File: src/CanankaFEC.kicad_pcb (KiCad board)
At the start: 2 copper layers, 24 x 27.9 mm, 26 parts, among them J1 B3B-XH-A, P1 105444-0001, U1 FT232RL, U2 PIC18F25K80

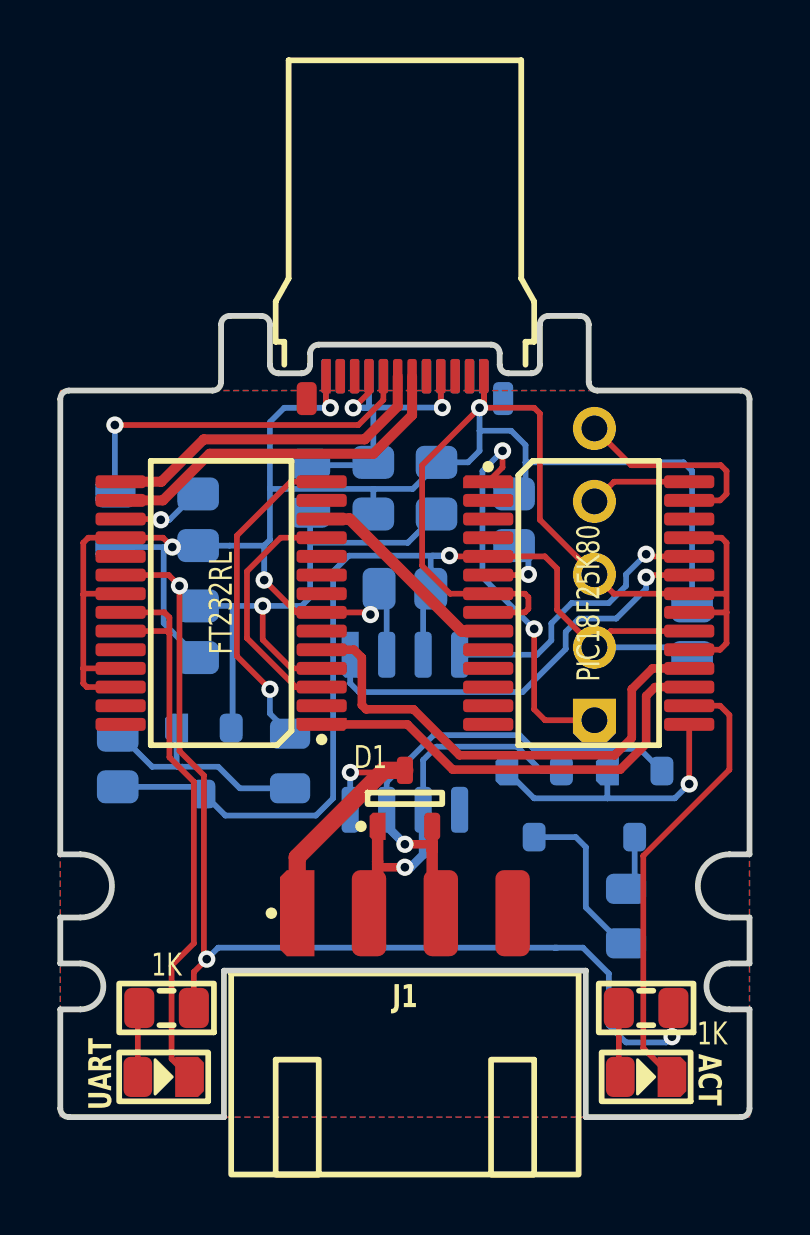
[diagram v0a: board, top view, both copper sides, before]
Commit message: Moved LEDs to bottom side
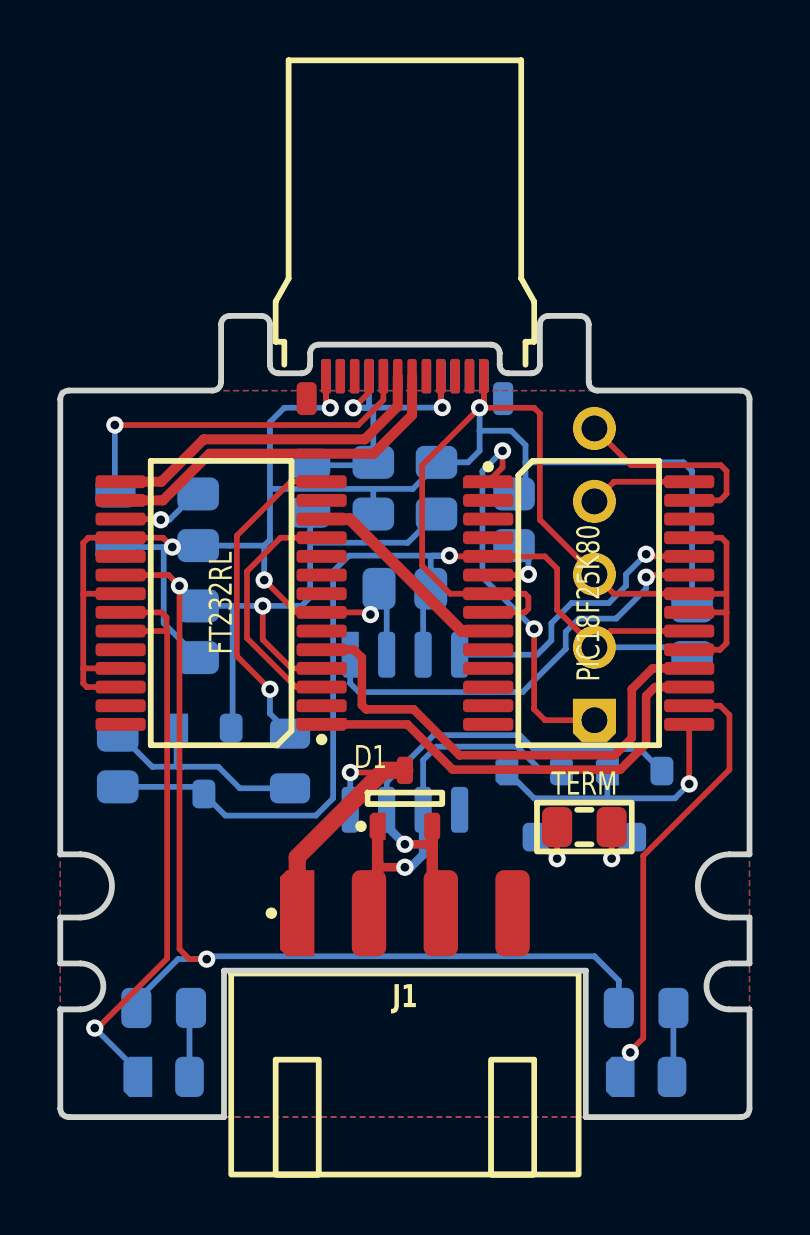
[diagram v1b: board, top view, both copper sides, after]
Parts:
- DS1, DS2, R2, R3: moved to B.Cu
- R1: value 120 -> TERM; moved to F.Cu
- moved R1 3.42 mm to (38.2, 37.8), turned to 0 degrees
- moved R2 0.10 mm to (23.6, 44.1), turned to 0 degrees
- turned DS1 to 0 degrees
- turned DS2 to 0 degrees
- turned R3 to 0 degrees
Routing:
- net CAN_L_TERM: track 5.96 -> 2.71 mm, vias 0 -> 1
- net 5V: track 58.1 -> 55.3 mm, vias 4 -> 3
- net GND: track 111.9 -> 109.8 mm
- net 5V_SW: track 38.9 -> 37.6 mm
- net CANH: track 17.4 -> 16.3 mm
- net LED_ACTIVITY: track 15.8 -> 15.2 mm, vias 0 -> 1
- net LED_UART: track 20.4 -> 20.8 mm, vias 0 -> 1
- net CAN_H_TERM: track 1.92 -> 2.21 mm, vias 0 -> 1

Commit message: Added PWREN pullup and moved LED 5V to switched
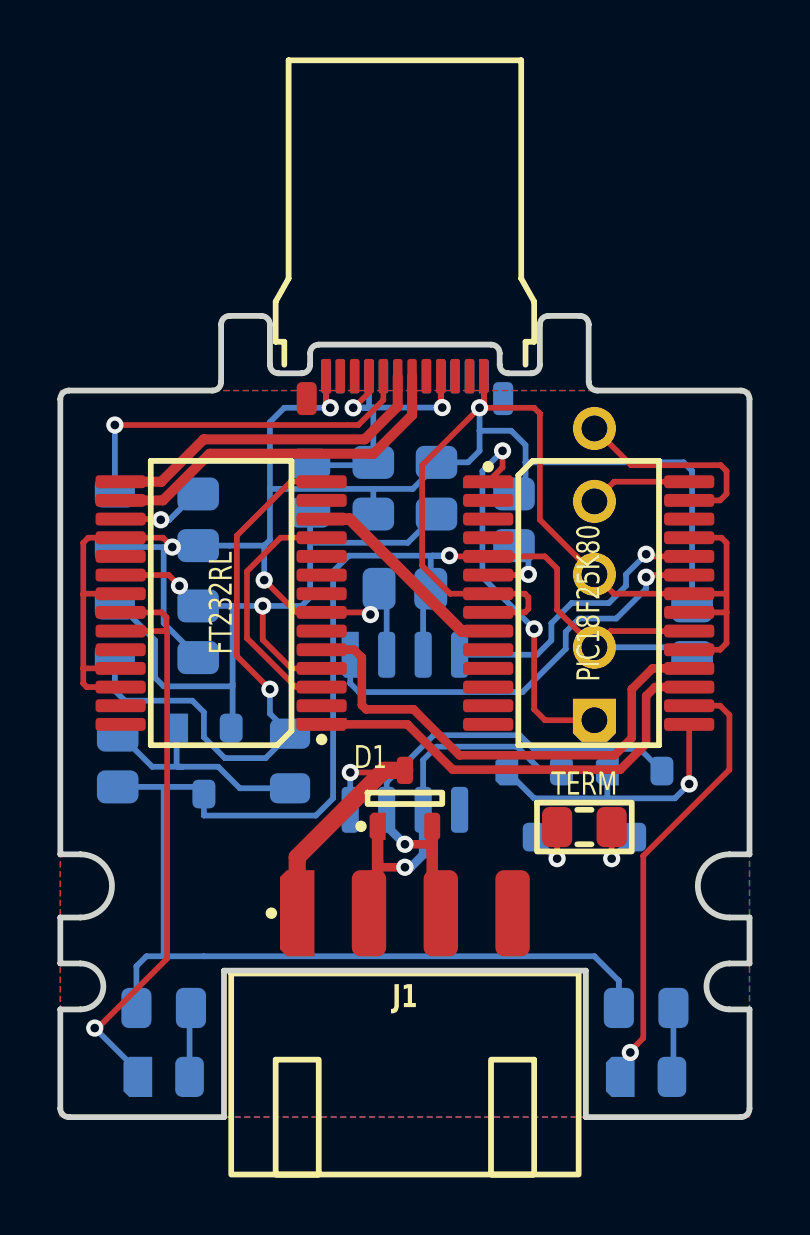
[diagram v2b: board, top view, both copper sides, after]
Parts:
- added R5: 10K, Medo64:R (0805), B.Cu at (21.9, 31.0)
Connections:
- R2 pad 1: 5V -> 5V_SW
- R3 pad 1: 5V -> 5V_SW
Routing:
- net 5V: track 55.3 -> 28.7 mm, vias 3 -> 2
- net 5V_SW: track 37.6 -> 63.4 mm
- net PWREN#: track 11.4 -> 20.4 mm

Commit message: Refactoring copper pour
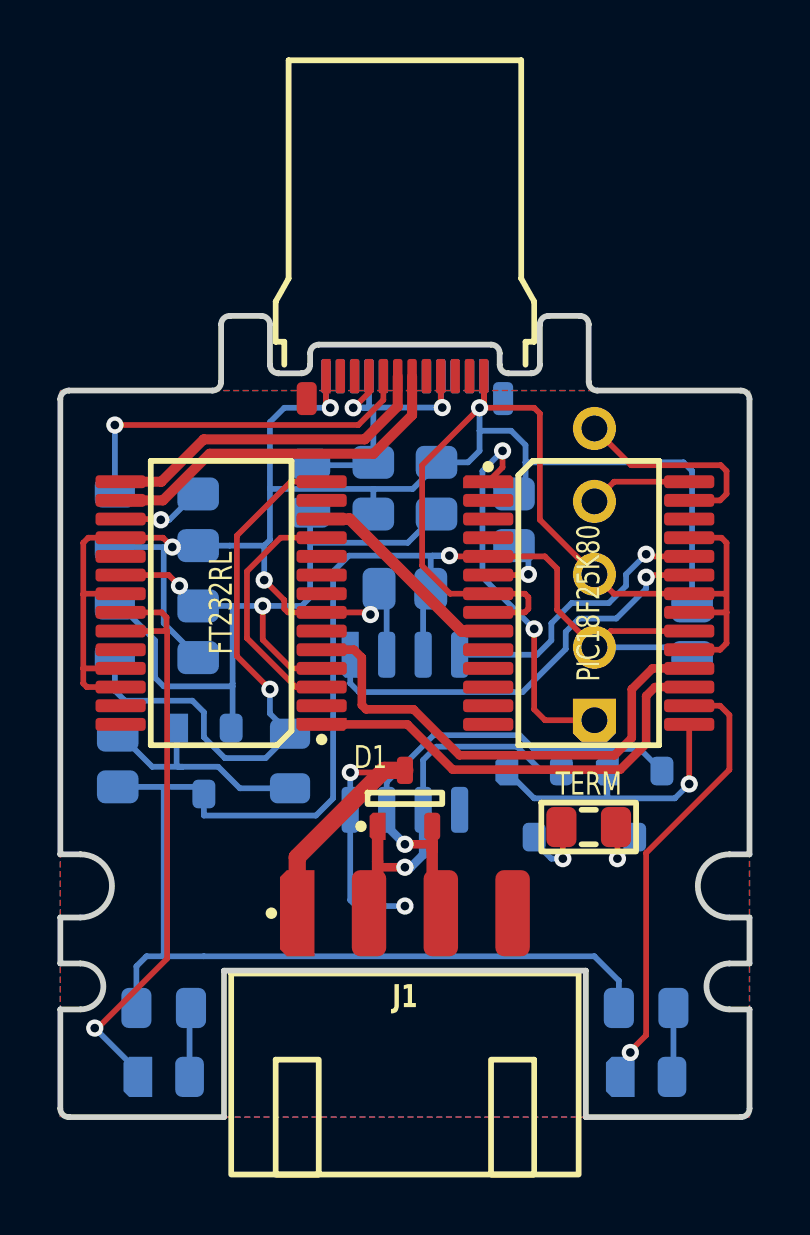
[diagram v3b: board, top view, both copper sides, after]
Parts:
- moved R1 0.15 mm to (38.4, 37.8)
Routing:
- net GND: track 109.8 -> 115.1 mm, vias 6 -> 7
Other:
- rule pad_to_mask_clearance: 0 -> 0.05
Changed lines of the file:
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@@
       (dielectric_constraints no)
     )
-    (pad_to_mask_clearance 0)
+    (pad_to_mask_clearance 0.05)
     (aux_axis_origin 20 20)
     (pcbplotparams
@@
   )
   (footprint "Medo64:R (0805)" (layer "F.Cu")
-    (at 38.25 37.8)
+    (at 38.4 37.8)
     (tags "RESC2013X70N")
     (attr smd)
@@
   (segment (start 36.175 30.325) (end 36.3 30.2) (width 0.2) (layer "F.Cu") (net 7))
   (segment (start 34.9 29.675) (end 33.575 29.675) (width 0.2) (layer "F.Cu") (net 7))
-  (segment (start 29.1 30.325) (end 28.225 30.325) (width 0.2) (layer "F.Cu") (net 7))
   (segment (start 34.75 22.95697) (end 34.75 22.1) (width 0.2) (layer "F.Cu") (net 7))
   (segment (start 22.1 32.275) (end 20.8 32.275) (width 0.2) (layer "F.Cu") (net 7))
@@
   (segment (start 32.6 25.2) (end 34.6 23.2) (width 0.2) (layer "F.Cu") (net 7))
   (segment (start 38.6 29) (end 36.7 27.1) (width 0.2) (layer "F.Cu") (net 7))
+  (segment (start 29.1 30.325) (end 27.925 30.325) (width 0.2) (layer "F.Cu") (net 7))
   (segment (start 43.2 27.9) (end 43.025 27.725) (width 0.2) (layer "F.Cu") (net 7))
   (segment (start 22.1 32.925) (end 20.925 32.925) (width 0.2) (layer "F.Cu") (net 7))
@@
   (segment (start 29.25 22.1) (end 29.25 23.05) (width 0.2) (layer "F.Cu") (net 7))
   (segment (start 34.50697 23.2) (end 34.75 22.95697) (width 0.2) (layer "F.Cu") (net 7))
+  (segment (start 27.925 30.325) (end 27.8 30.2) (width 0.2) (layer "F.Cu") (net 7))
   (segment (start 41.9 29.675) (end 39.275 29.675) (width 0.2) (layer "F.Cu") (net 7))
+  (segment (start 27.8 30.2) (end 27.8 29.9) (width 0.2) (layer "F.Cu") (net 7))
   (segment (start 20.8 32.275) (end 20.8 29.7) (width 0.2) (layer "F.Cu") (net 7))
-  (segment (start 28.225 30.325) (end 27.1 29.2) (width 0.2) (layer "F.Cu") (net 7))
+  (segment (start 27.8 29.9) (end 27.1 29.2) (width 0.2) (layer "F.Cu") (net 7))
   (segment (start 36.3 30.2) (end 36.3 29.8) (width 0.2) (layer "F.Cu") (net 7))
   (segment (start 28.25 38.85) (end 31.275 35.825) (width 0.6) (layer "F.Cu") (net 7))
@@
   (via (at 34.6 23.2) (size 0.6) (drill 0.3) (layers "F.Cu" "B.Cu") (net 7))
   (via (at 30.1 35.9) (size 0.6) (drill 0.3) (layers "F.Cu" "B.Cu") (net 7))
+  (via (at 32 40.55) (size 0.6) (drill 0.3) (layers "F.Cu" "B.Cu") (net 7))
   (segment (start 25.9 28) (end 24.8 28) (width 0.2) (layer "B.Cu") (net 7))
   (segment (start 30.095 35.905) (end 30.1 35.9) (width 0.2) (layer "B.Cu") (net 7))
   (segment (start 30.095 37.2) (end 30.095 35.905) (width 0.2) (layer "B.Cu") (net 7))
+  (segment (start 30.3 40.55) (end 32 40.55) (width 0.2) (layer "B.Cu") (net 7))
   (segment (start 36.2 25.1) (end 36.2 24.5) (width 0.2) (layer "B.Cu") (net 7))
   (segment (start 34.6 24.7) (end 34.6 24) (width 0.2) (layer "B.Cu") (net 7))
@@
   (segment (start 34.6 24) (end 34.6 23.2) (width 0.2) (layer "B.Cu") (net 7))
   (segment (start 35.7 24) (end 34.6 24) (width 0.2) (layer "B.Cu") (net 7))
+  (segment (start 30.095 40.345) (end 30.3 40.55) (width 0.2) (layer "B.Cu") (net 7))
   (segment (start 36.2 24.5) (end 35.7 24) (width 0.2) (layer "B.Cu") (net 7))
   (segment (start 34.75 22.1) (end 34.75 23.05) (width 0.2) (layer "B.Cu") (net 7))
@@
   (segment (start 30.9 26.025) (end 27.325 26.025) (width 0.2) (layer "B.Cu") (net 7))
   (segment (start 34.75 23.05) (end 34.6 23.2) (width 0.2) (layer "B.Cu") (net 7))
+  (segment (start 30.095 37.2) (end 30.095 40.345) (width 0.2) (layer "B.Cu") (net 7))
   (segment (start 27.325 26.025) (end 27.3 26) (width 0.2) (layer "B.Cu") (net 7))
   (segment (start 27.3 27.8) (end 27.3 26) (width 0.2) (layer "B.Cu") (net 7))
@@
   (segment (start 22.7 46.3) (end 21.2 44.8) (width 0.2) (layer "B.Cu") (net 20))
   (segment (start 24.5 46.5) (end 24.5 44.15) (width 0.2) (layer "B.Cu") (net 21))
+  (segment (start 40.4 38.701103) (end 43.3 35.801103) (width 0.2) (layer "F.Cu") (net 22))
   (segment (start 42.975 33.575) (end 41.9 33.575) (width 0.2) (layer "F.Cu") (net 22))
+  (segment (start 40.4 45.05) (end 40.4 38.701103) (width 0.2) (layer "F.Cu") (net 22))
+  (segment (start 39.85 45.6) (end 40.4 45.05) (width 0.2) (layer "F.Cu") (net 22))
+  (segment (start 43.3 33.9) (end 42.975 33.575) (width 0.2) (layer "F.Cu") (net 22))
   (segment (start 43.3 35.801103) (end 43.3 33.9) (width 0.2) (layer "F.Cu") (net 22))
-  (segment (start 40.3 45.15) (end 40.3 38.801103) (width 0.2) (layer "F.Cu") (net 22))
-  (segment (start 40.3 38.801103) (end 43.3 35.801103) (width 0.2) (layer "F.Cu") (net 22))
-  (segment (start 39.85 45.6) (end 40.3 45.15) (width 0.2) (layer "F.Cu") (net 22))
-  (segment (start 43.3 33.9) (end 42.975 33.575) (width 0.2) (layer "F.Cu") (net 22))
   (via (at 39.85 45.65) (size 0.6) (drill 0.3) (layers "F.Cu" "B.Cu") (net 22))
   (segment (start 39.85 46.15) (end 39.85 45.65) (width 0.2) (layer "B.Cu") (net 22))
@@
   (segment (start 36.3 28.5) (end 35.8 28) (width 0.2) (layer "B.Cu") (net 27))
   (segment (start 41.35 44.1) (end 41.35 46.45) (width 0.2) (layer "B.Cu") (net 28))
-  (segment (start 37.3 38.9) (end 37.3 37.8) (width 0.2) (layer "F.Cu") (net 29))
-  (via (at 37.3 38.9) (size 0.6) (drill 0.3) (layers "F.Cu" "B.Cu") (net 29))
-  (segment (start 37.25 38.9) (end 36.5 38.15) (width 0.2) (layer "B.Cu") (net 29))
-  (segment (start 37.3 38.9) (end 37.25 38.9) (width 0.2) (layer "B.Cu") (net 29))
-  (segment (start 39.2 37.8) (end 39.2 38.9) (width 0.2) (layer "F.Cu") (net 30))
-  (via (at 39.2 38.9) (size 0.6) (drill 0.3) (layers "F.Cu" "B.Cu") (net 30))
-  (segment (start 39.95 38.15) (end 39.2 38.9) (width 0.2) (layer "B.Cu") (net 30))
+  (segment (start 37.5 38.7) (end 37.5 38) (width 0.2) (layer "F.Cu") (net 29))
+  (via (at 37.5 38.9) (size 0.6) (drill 0.3) (layers "F.Cu" "B.Cu") (net 29))
+  (segment (start 37.1 38.9) (end 36.5 38.3) (width 0.2) (layer "B.Cu") (net 29))
+  (segment (start 37.5 38.9) (end 37.1 38.9) (width 0.2) (layer "B.Cu") (net 29))
+  (segment (start 39.4 37.85) (end 39.4 38.9) (width 0.2) (layer "F.Cu") (net 30))
+  (via (at 39.4 38.9) (size 0.6) (drill 0.3) (layers "F.Cu" "B.Cu") (net 30))
+  (segment (start 39.95 38.35) (end 39.4 38.9) (width 0.2) (layer "B.Cu") (net 30))
   (zone (net 7) (net_name "GND") (layers "F&B.Cu") (hatch edge 0.5)
-    (connect_pads (clearance 0.25))
-    (min_thickness 0.25) (filled_areas_thickness no)
+    (connect_pads no (clearance 0.3))
+    (min_thickness 0.3) (filled_areas_thickness no)
     (fill yes (thermal_gap 0.5) (thermal_bridge_width 0.5))
     (polygon
